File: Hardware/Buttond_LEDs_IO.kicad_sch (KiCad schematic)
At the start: 14 parts, among them J13 SFH11-PBPC-D05-ST-BK, SW1 RESET, SW2 BOOT

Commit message: small fixes
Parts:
- C18: Manufactuerer (none) -> TAIYO YUDEN; P/N (none) -> MLASH168SB7104KTNA01
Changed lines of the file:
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@@
 			)
 		)
-		(property "Datasheet" "~"
+		(property "Datasheet" "https://ds.yuden.co.jp/TYCOMPAS/or/download?pn=MLAST063SCG681JFNA01&fileType=CA"
 			(at 53.34 77.47 0)
 			(effects
@@
 			)
 		)
-		(property "Manufactuerer" ""
+		(property "Manufactuerer" "TAIYO YUDEN "
 			(at 53.34 77.47 0)
 			(effects
+				(font
+					(size 1.27 1.27)
+				)
+				(hide yes)
+			)
+		)
+		(property "P/N" "MLASH168SB7104KTNA01 "
+			(at 53.34 77.47 0)
+			(effects

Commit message: added BOM
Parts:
- J13: Manufactuerer (none) -> Sullins Connector Solutions
- LV1, LV2, LV3, LV4: Manufactuerer (none) -> NATIONSTAR; P/N (none) -> NCD0603R1
- R22, R23: Manufactuerer (none) -> Vishay; P/N (none) -> CRCW060310K0FKEI
- R24, R25, R26, R27: Manufactuerer (none) -> Vishay; P/N (none) -> CRCW0603120RFKEC
- SW1: Manufactuerer (none) -> Omron Electronics; P/N (none) -> B3SL-1002P
- SW2: Manufactuerer (none) -> Nidec Components; P/N (none) -> CJS-1200TA
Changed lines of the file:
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@@
 			)
 		)
-		(property "Datasheet" "~"
+		(property "Datasheet" "https://www.nidec-copal-electronics.com/e/catalog/switch/cjs.pdf"
 			(at 63.5 121.92 0)
 			(effects
@@
 			)
 		)
-		(property "Manufactuerer" ""
+		(property "Manufactuerer" "Nidec Components "
+			(at 63.5 114.3 0)
+			(effects
+				(font
+					(size 1.27 1.27)
+				)
+				(hide yes)
+			)
+		)
+		(property "P/N" "CJS-1200TA "
 			(at 63.5 114.3 0)
 			(effects
@@
 			)
 		)
-		(property "Datasheet" "~"
+		(property "Datasheet" "https://www.lcsc.com/datasheet/C84263.pdf"
 			(at 121.285 101.6 0)
 			(effects
@@
 			)
 		)
-		(property "Manufactuerer" ""
+		(property "Manufactuerer" "NATIONSTAR"
+			(at 121.285 101.6 90)
+			(effects
+				(font
+					(size 1.27 1.27)
+				)
+				(hide yes)
+			)
+		)
+		(property "P/N" "NCD0603R1"
 			(at 121.285 101.6 90)
 			(effects
@@
 			)
 		)
-		(property "Datasheet" "~"
+		(property "Datasheet" "https://www.vishay.com/docs/20035/dcrcwe3.pdf"
 			(at 121.285 92.71 0)
 			(effects
@@
 			)
 		)
-		(property "Manufactuerer" ""
+		(property "Manufactuerer" "Vishay "
+			(at 121.285 92.71 0)
+			(effects
+				(font
+					(size 1.27 1.27)
+				)
+				(hide yes)
+			)
+		)
+		(property "P/N" "CRCW0603120RFKEC "
 			(at 121.285 92.71 0)
 			(effects
@@
 			)
 		)
-		(property "Datasheet" "~"
+		(property "Datasheet" "https://www.vishay.com/docs/20035/dcrcwe3.pdf"
 			(at 53.34 64.77 0)
 			(effects
@@
 			)
 		)
-		(property "Manufactuerer" ""
+		(property "Manufactuerer" "Vishay "
+			(at 53.34 64.77 0)
+			(effects
+				(font
+					(size 1.27 1.27)
+				)
+				(hide yes)
+			)
+		)
+		(property "P/N" "CRCW060310K0FKEI "
 			(at 53.34 64.77 0)
 			(effects
@@
 			)
 		)
-		(property "Datasheet" "~"
+		(property "Datasheet" "https://www.vishay.com/docs/20035/dcrcwe3.pdf"
 			(at 132.715 92.71 0)
 			(effects
@@
 			)
 		)
-		(property "Manufactuerer" ""
+		(property "Manufactuerer" "Vishay "
+			(at 132.715 92.71 0)
+			(effects
+				(font
+					(size 1.27 1.27)
+				)
+				(hide yes)
+			)
+		)
+		(property "P/N" "CRCW0603120RFKEC "
 			(at 132.715 92.71 0)
 			(effects
@@
 			)
 		)
-		(property "Datasheet" "~"
+		(property "Datasheet" "https://www.lcsc.com/datasheet/C84263.pdf"
 			(at 132.715 101.6 0)
 			(effects
@@
 			)
 		)
-		(property "Manufactuerer" ""
+		(property "Manufactuerer" "NATIONSTAR"
+			(at 132.715 101.6 90)
+			(effects
+				(font
+					(size 1.27 1.27)
+				)
+				(hide yes)
+			)
+		)
+		(property "P/N" "NCD0603R1"
 			(at 132.715 101.6 90)
 			(effects
@@
 			)
 		)
-		(property "Datasheet" "~"
+		(property "Datasheet" "https://www.vishay.com/docs/20035/dcrcwe3.pdf"
 			(at 144.145 92.71 0)
 			(effects
@@
 			)
 		)
-		(property "Manufactuerer" ""
+		(property "Manufactuerer" "Vishay "
+			(at 144.145 92.71 0)
+			(effects
+				(font
+					(size 1.27 1.27)
+				)
+				(hide yes)
+			)
+		)
+		(property "P/N" "CRCW0603120RFKEC "
 			(at 144.145 92.71 0)
 			(effects
@@
 			)
 		)
-		(property "Datasheet" "https://www.digikey.com/en/products/detail/sullins-connector-solutions/SFH11-PBPC-D05-ST-BK/1990087?gclsrc=aw.ds&gad_source=1&gad_campaignid=120565755&gbraid=0AAAAADrbLljEsXDDEt5svizMM4jeYrL-A&gclid=Cj0KCQjwwZDFBhCpARIsAB95qO2YCKMg2VQme3QQBBCFa3dTLVMMS-qCbMZE8KZJpYe-_Bi6ULwi-x0aAvv3EALw_wcB"
+		(property "Datasheet" "https://s3.amazonaws.com/catalogspreads-pdf/PAGE123%20.100%20SFH11%20SERIES%20FEMALE%20HDR%20ST%20RA.pdf"
 			(at 234.315 90.805 0)
 			(effects
@@
 			)
 		)
-		(property "Manufactuerer" ""
+		(property "Manufactuerer" "Sullins Connector Solutions"
 			(at 234.315 90.805 0)
 			(effects
@@
 			)
 		)
-		(property "Datasheet" "~"
+		(property "Datasheet" "https://www.vishay.com/docs/20035/dcrcwe3.pdf"
 			(at 155.575 92.71 0)
 			(effects
@@
 			)
 		)
-		(property "Manufactuerer" ""
+		(property "Manufactuerer" "Vishay "
+			(at 155.575 92.71 0)
+			(effects
+				(font
+					(size 1.27 1.27)
+				)
+				(hide yes)
+			)
+		)
+		(property "P/N" "CRCW0603120RFKEC "
 			(at 155.575 92.71 0)
 			(effects
@@
 			)
 		)
-		(property "Datasheet" "http://www.apem.com/int/index.php?controller=attachment&id_attachment=488"
+		(property "Datasheet" "https://www.omron.com/ecb/products/pdf/en-b3sl.pdf"
 			(at 63.5 67.31 0)
 			(effects
@@
 			)
 		)
-		(property "Manufactuerer" ""
+		(property "Manufactuerer" "Omron Electronics "
+			(at 63.5 72.39 0)
+			(effects
+				(font
+					(size 1.27 1.27)
+				)
+				(hide yes)
+			)
+		)
+		(property "P/N" "B3SL-1002P "
 			(at 63.5 72.39 0)
 			(effects
@@
 			)
 		)
-		(property "Datasheet" "~"
+		(property "Datasheet" "https://www.lcsc.com/datasheet/C84263.pdf"
 			(at 155.575 101.6 0)
 			(effects
@@
 			)
 		)
-		(property "Manufactuerer" ""
+		(property "Manufactuerer" "NATIONSTAR"
+			(at 155.575 101.6 90)
+			(effects
+				(font
+					(size 1.27 1.27)
+				)
+				(hide yes)
+			)
+		)
+		(property "P/N" "NCD0603R1"
 			(at 155.575 101.6 90)
 			(effects
@@
 			)
 		)
-		(property "Datasheet" "~"
+		(property "Datasheet" "https://www.lcsc.com/datasheet/C84263.pdf"
 			(at 144.145 101.6 0)
 			(effects
@@
 			)
 		)
-		(property "Manufactuerer" ""
+		(property "Manufactuerer" "NATIONSTAR"
+			(at 144.145 101.6 90)
+			(effects
+				(font
+					(size 1.27 1.27)
+				)
+				(hide yes)
+			)
+		)
+		(property "P/N" "NCD0603R1"
 			(at 144.145 101.6 90)
 			(effects
@@
 			)
 		)
-		(property "Datasheet" "~"
+		(property "Datasheet" "https://www.vishay.com/docs/20035/dcrcwe3.pdf"
 			(at 52.705 114.3 0)
 			(effects
@@
 			)
 		)
-		(property "Manufactuerer" ""
+		(property "Manufactuerer" "Vishay "
 			(at 52.705 114.3 90)
 			(effects
+				(font
+					(size 1.27 1.27)
+				)
+				(hide yes)
+			)
+		)
+		(property "P/N" "CRCW060310K0FKEI "
+			(at 52.705 114.3 90)
+			(effects

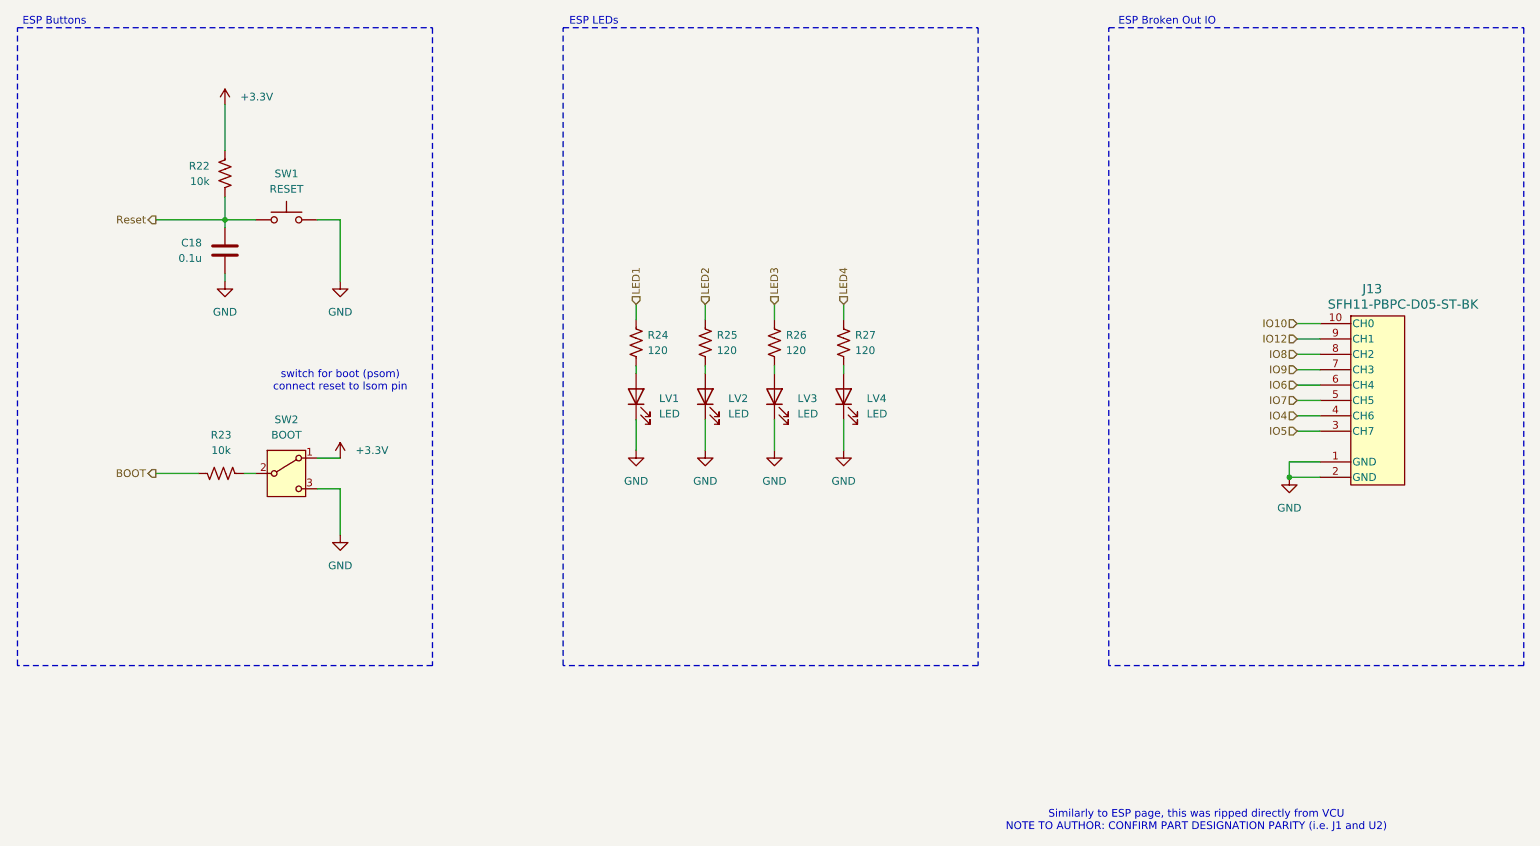
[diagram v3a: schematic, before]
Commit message: RevB PR (#14)
* RevB Schematic Update

* RevB Schematic revisions

* revB updates

* Schematic polishes, layout WIP

* circuit blocks designed, schematic updated

* unblocked SD card holder

* halfway laid-out

* unblocked SD card again

* small schematic changes

* intial layout design

* Updated LSOM footprint

* filled in copper holes. Name/REV/Date added

* RevB layout completed

* JLC Production Files

* added resistors

* replace silkscreen

* condensed custom lirbraries

* removed all unnessasary files and some nessasary ones
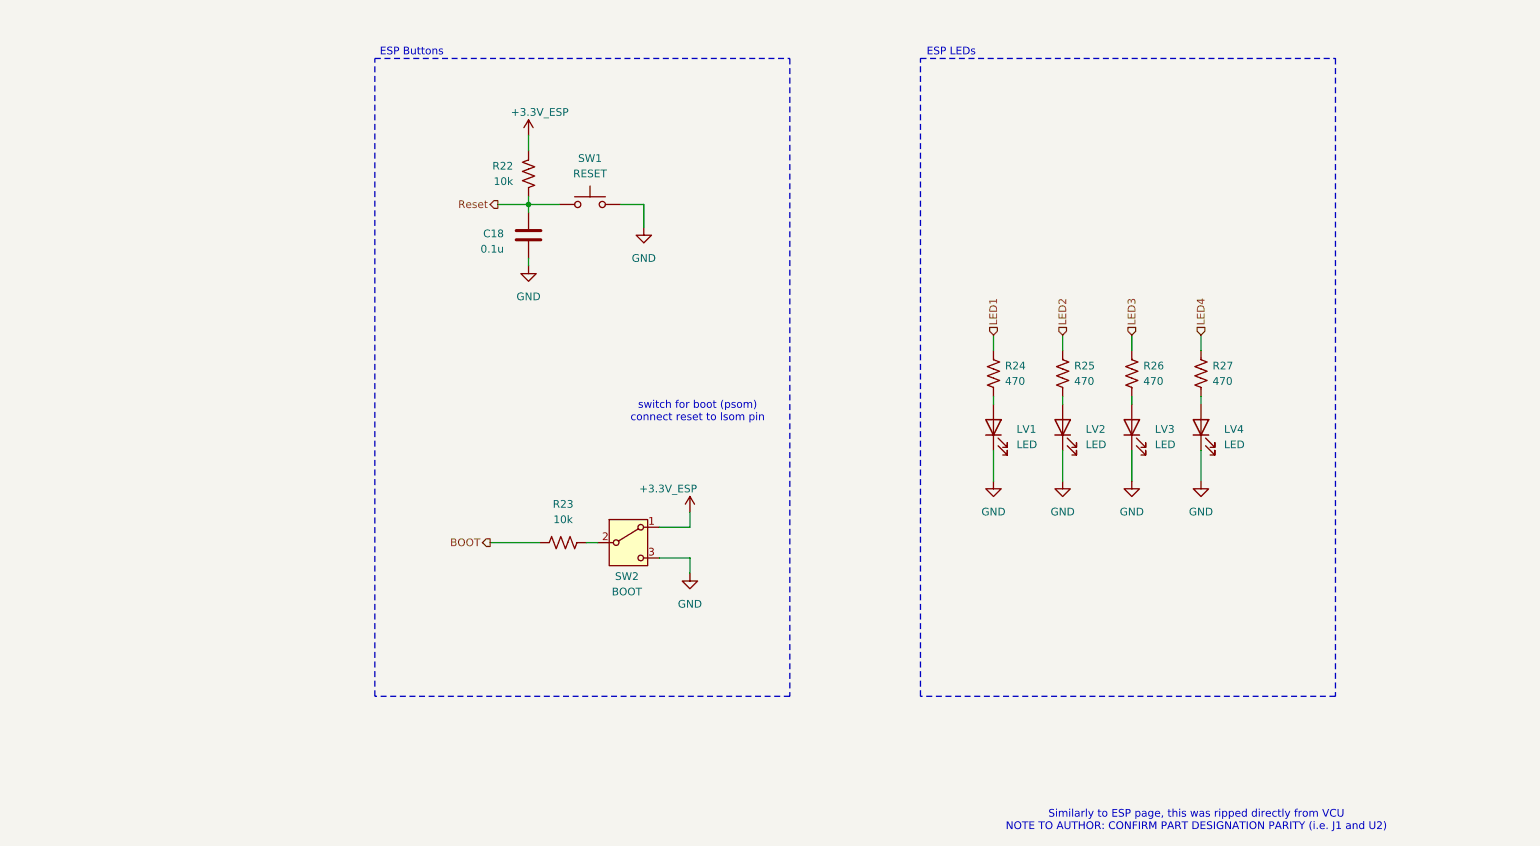
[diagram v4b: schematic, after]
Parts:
- removed J13: SFH11-PBPC-D05-ST-BK, UTSVT_Connectors:CONN_SFH11-xxxC-D05-ST-XX_SUL, symbol UTSVT_Connectors:SFH11-PBPC-D05-ST-BK
- C18: LCSC (none) -> C14663
- LV1, LV2, LV3, LV4: LCSC (none) -> C7371904
- R22, R23: LCSC (none) -> C25804
- R24, R25, R26, R27: value 120 -> 470; LCSC (none) -> C23179
- SW1: footprint UTSVT_Special:SW_SPST_B3SL-1002P -> CustomKiCad-Library:TL3365AF180QG; LCSC (none) -> C2886926
- SW2: LCSC (none) -> C2921628
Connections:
- net BOOT: now also R23.2; no longer R23.1
- net at SW2.2 (B): now also R23.1; no longer R23.2
- net +3.3V renamed +3.3V_ESP
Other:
- note removed: "ESP Broken Out IO"
- moved on the sheet: C18, LV1, LV2, LV3, LV4, R22, R23, R24, R25, R26, R27, SW1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
